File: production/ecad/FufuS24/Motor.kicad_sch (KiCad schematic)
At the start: 0 parts

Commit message: Motor Schematic V1
if you're reading this AAAAAAAAAAAAAAAAAAAAAAAAAAAAAAAAAAAAAAAAAAAAAAAAAAAAAAAAAAAAAAAAAAAAAA
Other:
- note added: "AOUT1"
- note added: "AOUT2"
- note added: "BEMF"
- note added: "BIN1"
- note added: "BIN2"
- note added: "BOUT1"
- note added: "BOUT2"
- note added: "DIR"
- note added: "FLT"
- note added: "GND"
- note added: "I ACTUALLY DON'T KNOW HOW MUCH OF A SCHEMATIC THIS IS A LOT OF IT IS AN FYI ETHAN PLEASE DON'T KILL ME"
- note added: "IOREF"
- note added: "PWM"
- note added: "RST"
- note added: "SCLK"
- note added: "SCS"
- note added: "SDATI"
- note added: "SDATO"
- note added: "SLP"
- note added: "SPI CLOCK"
- note added: "SPI CSn"
- note added: "SPI RX"
- note added: "SPI TX"
- note added: "STALL"
- note added: "STEP"
- note added: "TO STEPPER MOTOR LEAD A"
- note added: "TO STEPPER MOTOR LEAD B"
- note added: "TO STEPPER MOTOR LEAD C"
- note added: "TO STEPPER MOTOR LEAD D"
- note added: "V5_OUT"
- note added: "VIN"
- note added: "VM"

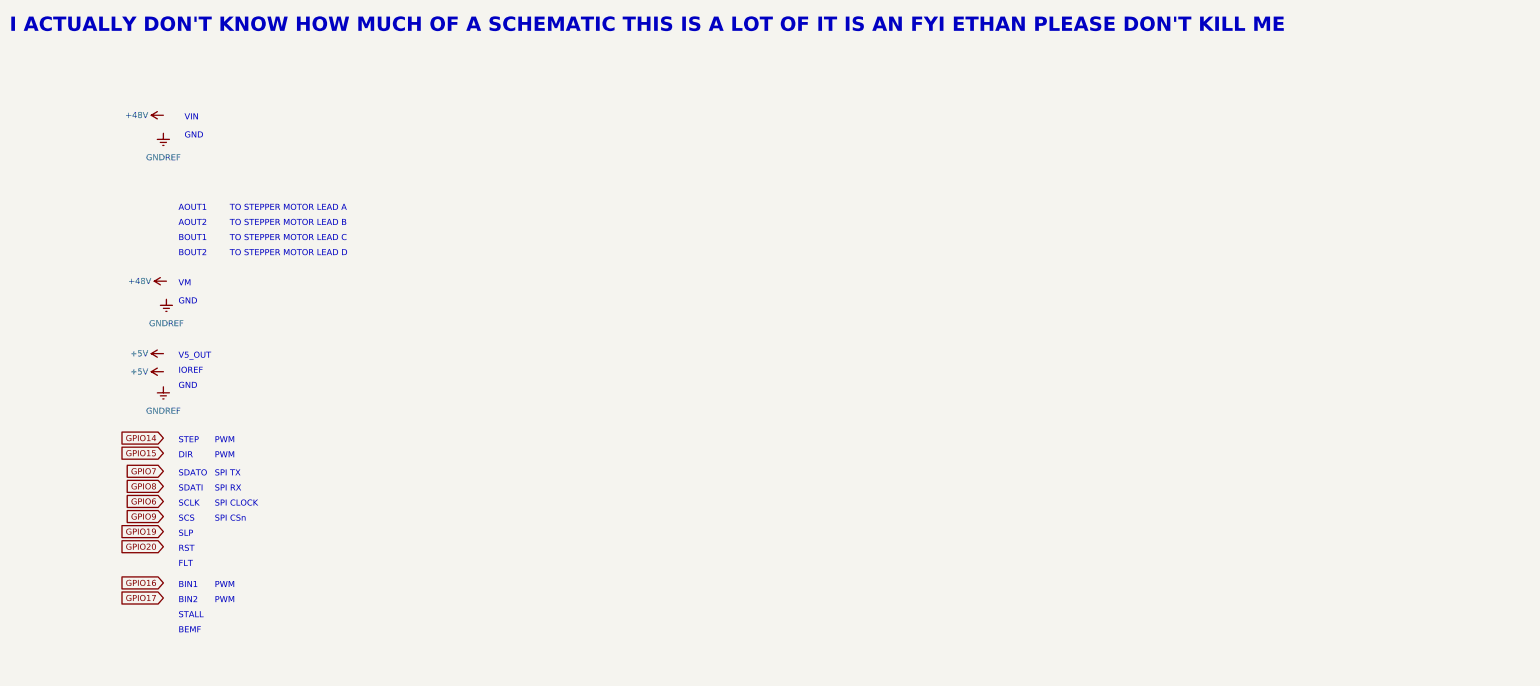
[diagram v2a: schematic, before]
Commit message: Updated Motor
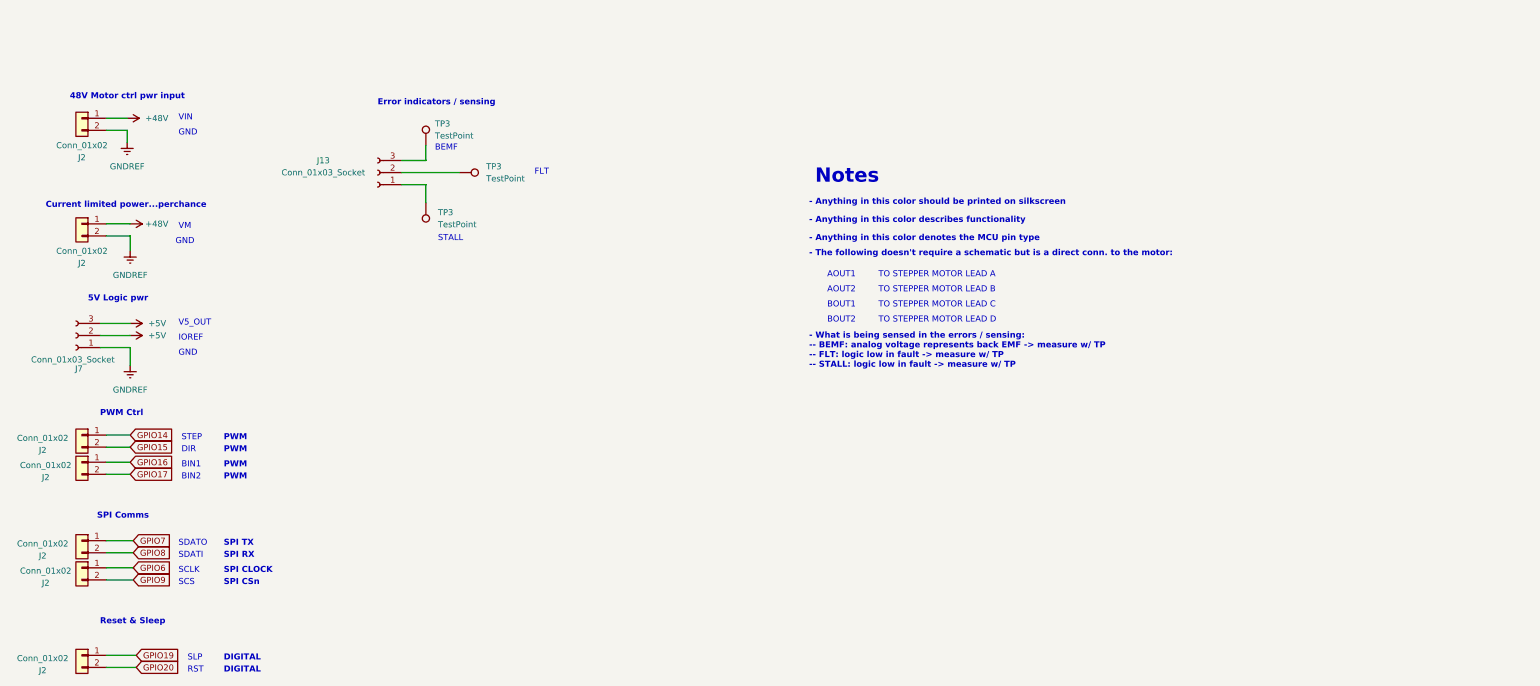
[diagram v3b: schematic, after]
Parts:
- added J13, J7: Conn_01x03_Socket, symbol Connector:Conn_01x03_Socket
- added J2 (x7): Conn_01x02, symbol Connector_Generic:Conn_01x02
- added TP3 (x3): TestPoint, TestPoint:TestPoint_Pad_2.0x2.0mm, symbol Connector:TestPoint
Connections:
- net +48V: now also J2.1 (Pin_1), J2.1 (Pin_1)
- net +5V: now also J7.2 (Pin_2), J7.3 (Pin_3)
- net GNDREF: now also J2.2 (Pin_2), J2.2 (Pin_2), J7.1 (Pin_1)
- net GPIO14: now also J2.1 (Pin_1)
- net GPIO15: now also J2.2 (Pin_2)
- net GPIO16: now also J2.1 (Pin_1)
- net GPIO17: now also J2.2 (Pin_2)
- net GPIO19: now also J2.1 (Pin_1)
- net GPIO20: now also J2.2 (Pin_2)
- net GPIO6: now also J2.1 (Pin_1)
- net GPIO7: now also J2.1 (Pin_1)
- net GPIO8: now also J2.2 (Pin_2)
- net GPIO9: now also J2.2 (Pin_2)
- new net: J13.2 (Pin_2), TP3.1
- new net: J13.1 (Pin_1), TP3.1
- new net: J13.3 (Pin_3), TP3.1
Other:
- note added: "- Anything in this color denotes the MCU pin type"
- note added: "- Anything in this color describes functionality"
- note added: "- Anything in this color should be printed on silkscreen"
- note added: "- The following doesn't require a schematic but is a direct conn. to the motor:"
- note added: "- What is being sensed in the errors / sensing: -- BEMF: analog voltage represents back EMF -> measure w/ TP -- FLT: logic low in fault -> measure w/ TP -- STALL: logic low in fault -> measure w/ TP"
- note added: "48V Motor ctrl pwr input"
- note added: "5V Logic pwr"
- note added: "Current limited power...perchance"
- note added: "DIGITAL"
- note added: "Error indicators / sensing"
- note added: "Notes"
- note added: "PWM Ctrl"
- note added: "Reset & Sleep"
- note added: "SPI Comms"
- note removed: "I ACTUALLY DON'T KNOW HOW MUCH OF A SCHEMATIC THIS IS A LOT OF IT IS AN FYI ETHAN PLEASE DON'T KILL ME"

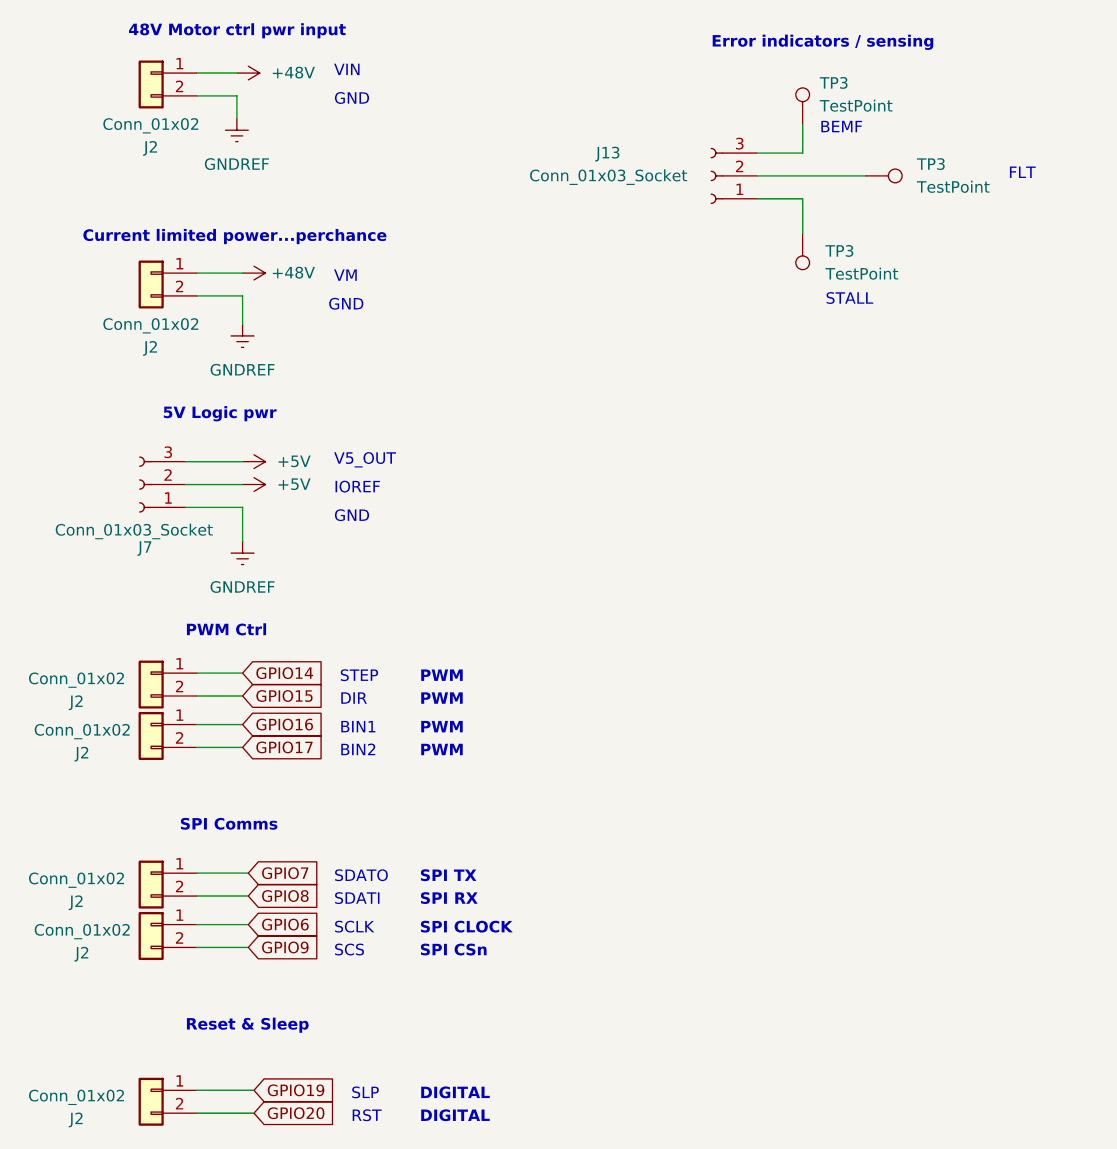
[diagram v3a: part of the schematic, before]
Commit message: Updated heating cap
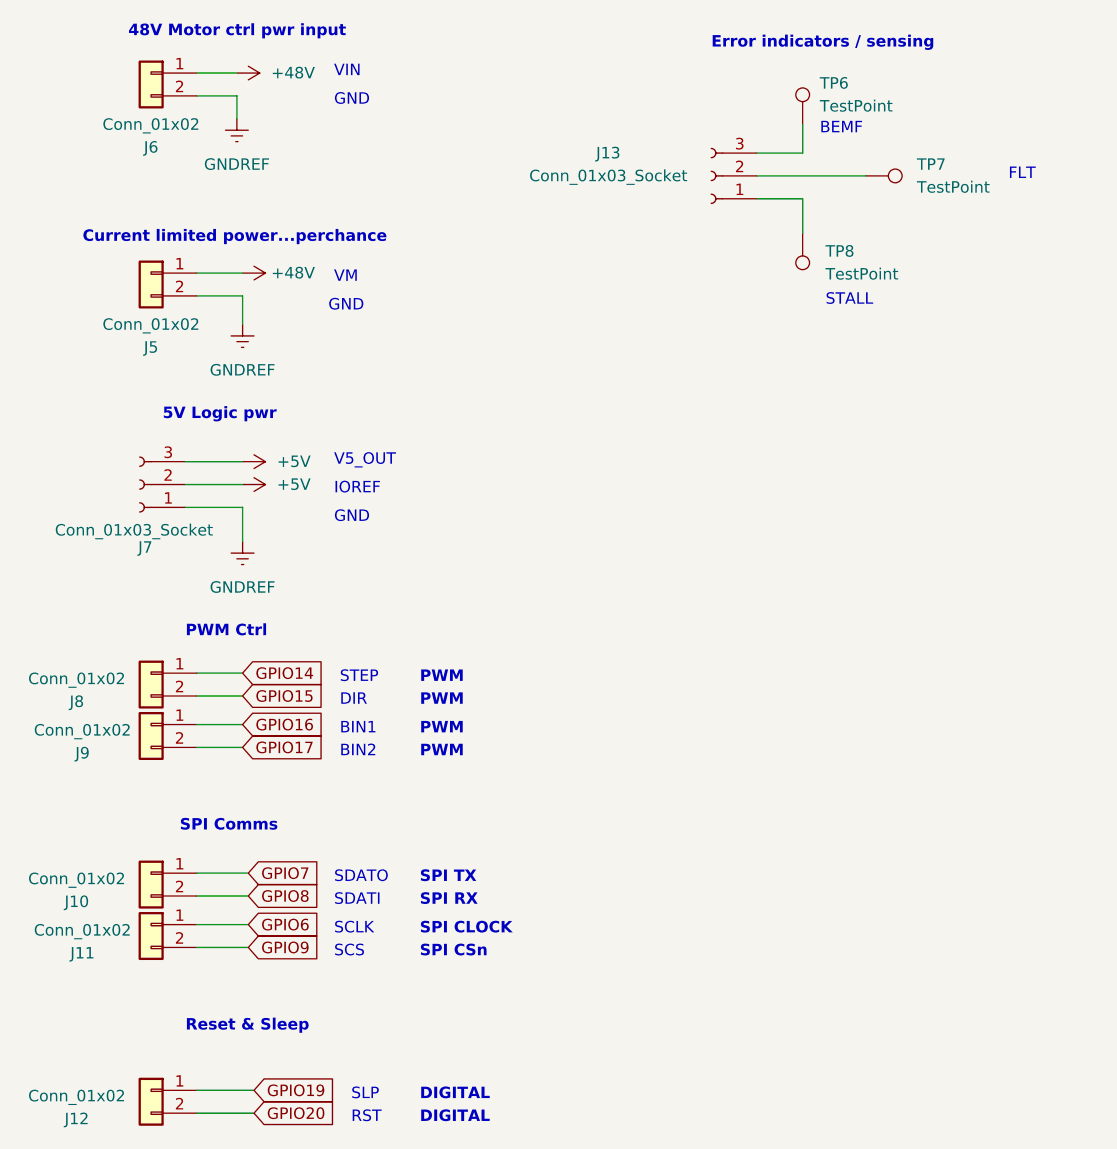
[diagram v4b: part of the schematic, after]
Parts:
- renumbered J2 to J10, J2 to J11, J2 to J12, J2 to J5, J2 to J6, J2 to J8, J2 to J9, TP3 to TP6, TP3 to TP7, TP3 to TP8
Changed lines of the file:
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@@
   (symbol (lib_id "Connector_Generic:Conn_01x02") (at 32.385 104.775 0) (mirror y) (unit 1)
     (in_bom yes) (on_board yes) (dnp no)
-    (property "Reference" "J2" (at 24.13 107.95 0)
+    (property "Reference" "J8" (at 24.13 107.95 0)
       (effects (font (size 1.27 1.27)))
     )
@@
     (instances
       (project "FufuS24"
-        (path "/c4c3980b-c8c0-435e-abdc-bbed2349d7ac/2f899246-8d98-4f9c-b4c6-8497c11eb038"
-          (reference "J2") (unit 1)
-        )
         (path "/c4c3980b-c8c0-435e-abdc-bbed2349d7ac/67add6e2-1584-4801-9b59-67cf5082dcca"
           (reference "J8") (unit 1)
@@
   (symbol (lib_id "Connector:TestPoint") (at 111.76 49.53 270) (unit 1)
     (in_bom yes) (on_board yes) (dnp no) (fields_autoplaced)
-    (property "Reference" "TP3" (at 117.475 48.26 90)
+    (property "Reference" "TP7" (at 117.475 48.26 90)
       (effects (font (size 1.27 1.27)) (justify left))
     )
@@
     (instances
       (project "FufuS24"
-        (path "/c4c3980b-c8c0-435e-abdc-bbed2349d7ac/1f62379a-1fa8-439b-93cd-7c736b3b1bba"
-          (reference "TP3") (unit 1)
-        )
         (path "/c4c3980b-c8c0-435e-abdc-bbed2349d7ac/67add6e2-1584-4801-9b59-67cf5082dcca"
           (reference "TP7") (unit 1)
@@
   (symbol (lib_id "Connector_Generic:Conn_01x02") (at 32.385 60.325 0) (mirror y) (unit 1)
     (in_bom yes) (on_board yes) (dnp no)
-    (property "Reference" "J2" (at 32.385 68.58 0)
+    (property "Reference" "J5" (at 32.385 68.58 0)
       (effects (font (size 1.27 1.27)))
     )
@@
     (instances
       (project "FufuS24"
-        (path "/c4c3980b-c8c0-435e-abdc-bbed2349d7ac/2f899246-8d98-4f9c-b4c6-8497c11eb038"
-          (reference "J2") (unit 1)
-        )
         (path "/c4c3980b-c8c0-435e-abdc-bbed2349d7ac/67add6e2-1584-4801-9b59-67cf5082dcca"
           (reference "J5") (unit 1)
@@
   (symbol (lib_id "Connector_Generic:Conn_01x02") (at 32.385 151.13 0) (mirror y) (unit 1)
     (in_bom yes) (on_board yes) (dnp no)
-    (property "Reference" "J2" (at 24.13 154.305 0)
+    (property "Reference" "J12" (at 24.13 154.305 0)
       (effects (font (size 1.27 1.27)))
     )
@@
     (instances
       (project "FufuS24"
-        (path "/c4c3980b-c8c0-435e-abdc-bbed2349d7ac/2f899246-8d98-4f9c-b4c6-8497c11eb038"
-          (reference "J2") (unit 1)
-        )
         (path "/c4c3980b-c8c0-435e-abdc-bbed2349d7ac/67add6e2-1584-4801-9b59-67cf5082dcca"
           (reference "J12") (unit 1)
@@
   (symbol (lib_id "Connector_Generic:Conn_01x02") (at 32.385 132.715 0) (mirror y) (unit 1)
     (in_bom yes) (on_board yes) (dnp no)
-    (property "Reference" "J2" (at 24.765 135.89 0)
+    (property "Reference" "J11" (at 24.765 135.89 0)
       (effects (font (size 1.27 1.27)))
     )
@@
     (instances
       (project "FufuS24"
-        (path "/c4c3980b-c8c0-435e-abdc-bbed2349d7ac/2f899246-8d98-4f9c-b4c6-8497c11eb038"
-          (reference "J2") (unit 1)
-        )
         (path "/c4c3980b-c8c0-435e-abdc-bbed2349d7ac/67add6e2-1584-4801-9b59-67cf5082dcca"
           (reference "J11") (unit 1)
@@
   (symbol (lib_id "Connector:TestPoint") (at 104.775 43.815 0) (unit 1)
     (in_bom yes) (on_board yes) (dnp no) (fields_autoplaced)
-    (property "Reference" "TP3" (at 106.68 39.243 0)
+    (property "Reference" "TP6" (at 106.68 39.243 0)
       (effects (font (size 1.27 1.27)) (justify left))
     )
@@
     (instances
       (project "FufuS24"
-        (path "/c4c3980b-c8c0-435e-abdc-bbed2349d7ac/1f62379a-1fa8-439b-93cd-7c736b3b1bba"
-          (reference "TP3") (unit 1)
-        )
         (path "/c4c3980b-c8c0-435e-abdc-bbed2349d7ac/67add6e2-1584-4801-9b59-67cf5082dcca"
           (reference "TP6") (unit 1)
@@
   (symbol (lib_id "Connector_Generic:Conn_01x02") (at 32.385 110.49 0) (mirror y) (unit 1)
     (in_bom yes) (on_board yes) (dnp no)
-    (property "Reference" "J2" (at 24.765 113.665 0)
+    (property "Reference" "J9" (at 24.765 113.665 0)
       (effects (font (size 1.27 1.27)))
     )
@@
     (instances
       (project "FufuS24"
-        (path "/c4c3980b-c8c0-435e-abdc-bbed2349d7ac/2f899246-8d98-4f9c-b4c6-8497c11eb038"
-          (reference "J2") (unit 1)
-        )
         (path "/c4c3980b-c8c0-435e-abdc-bbed2349d7ac/67add6e2-1584-4801-9b59-67cf5082dcca"
           (reference "J9") (unit 1)
@@
   (symbol (lib_id "Connector:TestPoint") (at 104.775 55.88 180) (unit 1)
     (in_bom yes) (on_board yes) (dnp no) (fields_autoplaced)
-    (property "Reference" "TP3" (at 107.315 57.912 0)
+    (property "Reference" "TP8" (at 107.315 57.912 0)
       (effects (font (size 1.27 1.27)) (justify right))
     )
@@
     (instances
       (project "FufuS24"
-        (path "/c4c3980b-c8c0-435e-abdc-bbed2349d7ac/1f62379a-1fa8-439b-93cd-7c736b3b1bba"
-          (reference "TP3") (unit 1)
-        )
         (path "/c4c3980b-c8c0-435e-abdc-bbed2349d7ac/67add6e2-1584-4801-9b59-67cf5082dcca"
           (reference "TP8") (unit 1)
@@
   (symbol (lib_id "Connector_Generic:Conn_01x02") (at 32.385 127 0) (mirror y) (unit 1)
     (in_bom yes) (on_board yes) (dnp no)
-    (property "Reference" "J2" (at 24.13 130.175 0)
+    (property "Reference" "J10" (at 24.13 130.175 0)
       (effects (font (size 1.27 1.27)))
     )
@@
     (instances
       (project "FufuS24"
-        (path "/c4c3980b-c8c0-435e-abdc-bbed2349d7ac/2f899246-8d98-4f9c-b4c6-8497c11eb038"
-          (reference "J2") (unit 1)
-        )
         (path "/c4c3980b-c8c0-435e-abdc-bbed2349d7ac/67add6e2-1584-4801-9b59-67cf5082dcca"
           (reference "J10") (unit 1)
@@
   (symbol (lib_id "Connector_Generic:Conn_01x02") (at 32.385 38.1 0) (mirror y) (unit 1)
     (in_bom yes) (on_board yes) (dnp no)
-    (property "Reference" "J2" (at 32.385 46.355 0)
+    (property "Reference" "J6" (at 32.385 46.355 0)
       (effects (font (size 1.27 1.27)))
     )
@@
     (instances
       (project "FufuS24"
-        (path "/c4c3980b-c8c0-435e-abdc-bbed2349d7ac/2f899246-8d98-4f9c-b4c6-8497c11eb038"
-          (reference "J2") (unit 1)
-        )
         (path "/c4c3980b-c8c0-435e-abdc-bbed2349d7ac/67add6e2-1584-4801-9b59-67cf5082dcca"
           (reference "J6") (unit 1)

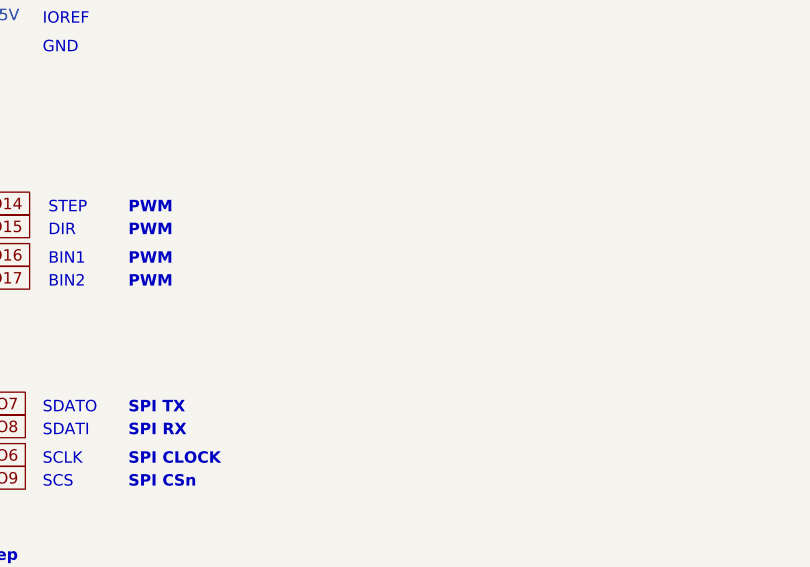
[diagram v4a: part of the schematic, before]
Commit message: Design review changes
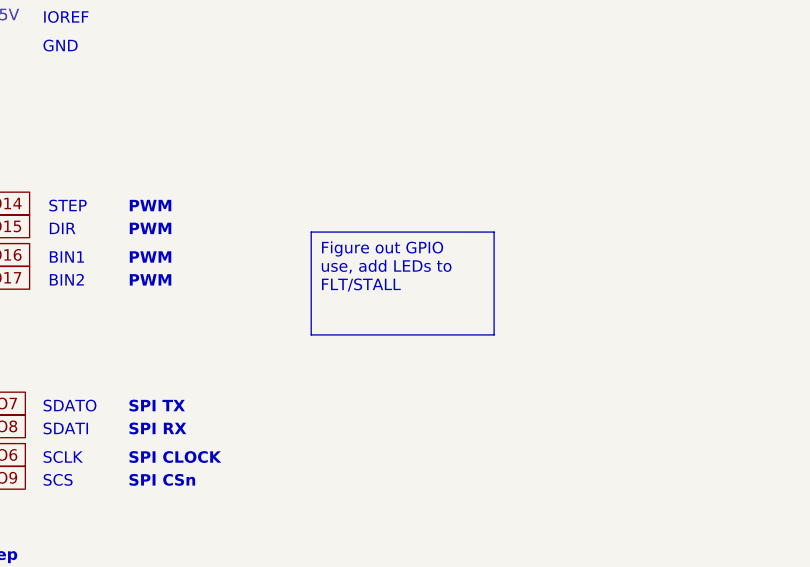
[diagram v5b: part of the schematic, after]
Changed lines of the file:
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@@
     (stroke (width 0) (type default))
+  )
+  (text_box "Figure out GPIO use, add LEDs to FLT/STALL"
+    (at 82.55 107.95 0) (size 20.32 11.43)
+    (stroke (width 0) (type default))
+    (fill (type none))
+    (effects (font (size 1.27 1.27)) (justify left top))
   )
   (text "- Anything in this color describes functionality" (at 185.42 60.325 0)
